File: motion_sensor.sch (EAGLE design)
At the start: 11 parts, among them U1 LP2985A-33DBVTE4

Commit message: Move away from esp8266 to ATMEGA328 + nRF8001
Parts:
- removed MDL1: (no value), ESP8266-ESP12E:ESP8266-12EESP8266-ESP12E
- added C1, C13, C14, C2: 15pF, microbuilder:CAP_CERAMIC0805-NOOUTLINE
- added C10: 0.1uF, microbuilder:CAP_CERAMIC0805-NOOUTLINE
- added C11: 33nF, microbuilder:CAP_CERAMIC0805-NOOUTLINE
- added C12, C4: 0.1µF, microbuilder:CAP_CERAMIC0805-NOOUTLINE
- added C15: 1.5pF, microbuilder:CAP_CERAMIC_0402MP
- added C16, C18: 22pF, SparkFun-Capacitors:22PF-50V-5%(0603)
- added C17, C9: 10µF, microbuilder:CAP_CERAMIC0805-NOOUTLINE
- added C3: 2.2nF, microbuilder:CAP_CERAMIC_0402
- added C5: 1.8pF, microbuilder:CAP_CERAMIC_0402MP
- added C6: 1.2pF, microbuilder:CAP_CERAMIC_0402MP
- added C7: 1µF, microbuilder:CAP_CERAMIC0805-NOOUTLINE
- added C8: 1nF, microbuilder:CAP_CERAMIC_0603
- added FB1: MMZ1608B121C, microbuilder:FERRITE0805
- added J1: AVR_SPI_PRG_6PTH, SparkFun-Connectors:AVR_SPI_PRG_6PTH
- added L1: 8.2nH, microbuilder:INDUCTOR_0402
- added L2: 5.6nH, microbuilder:INDUCTOR_0402
- added L3: 3.9nH, microbuilder:INDUCTOR_0402
- added L4: 10µH, microbuilder:INDUCTOR_0603
- added L5: 15nH, microbuilder:INDUCTOR_0603
- added R1: 22K, microbuilder:RESISTOR_0805MP
- added R2: 10K, SparkFun-Resistors:10KOHM-1/10W-1%(0603)0603
- added U$28: (no value), microbuilder:ANTENNA_PCBNRF8001_1.6MM
- added U2: nRF8001, microbuilder:NRF8001
- added U3: ATMEGA328P_TQFP, SparkFun-DigitalIC:ATMEGA328P_TQFP
- added Y1: 16MHz, microbuilder:CRYSTAL3.2X2.5
- added Y2: FC-255 32.7680K-A3, microbuilder:CRYSTAL8.0X3.8
- added Y3: (no value), SparkFun-FreqCtrl:CRYSTALSMD
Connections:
- removed net ADC: MDL1.ADC
- removed net RX: MDL1.RXD
- removed net TX: MDL1.TXD
- new net 5V: J1.2
- new net ACTIVE: U2A.ACTIVE
- new net AVDD: C4.1, C7.1, C8.1, FB1.P$2, L5.2, U2A.AVDD@1, U2A.AVDD@2, U2A.AVDD@3
- new net MISO: J1.1, U2A.MISO, U3.PB4(MISO)
- new net MOSI: J1.4, U3.PB3(MOSI/OC2)
- new net MOSI_3V: U2A.MOSI
- new net N$1: C11.1, U2A.DEC2
- new net N$10: C2.1, U2A.XC2, Y1.1
- new net N$11: L4.1, U2A.DCC
- new net N$17: L1.2, L3.1, U2A.ANT2
- new net N$18: L1.1, L2.1, U2A.ANT1
- new net N$19: C5.2, L3.2
- new net N$2: R1.1, U2A.IREF
- new net N$20: C15.2, C5.1, C6.2, U$28.P$1
- new net N$21: C16.1, U3.PB6(XTAL1/TOSC1), Y3.1
- new net N$22: C14.2, U2A.XL2, Y2.1
- new net N$23: C13.2, U2A.XL1, Y2.2
- new net N$26: R2.2, U3.PC6(/RESET)
- new net N$3: L4.2, L5.1
- new net N$4: C3.1, L2.2, U2A.VDD_PA
- new net N$8: C10.1, U2A.DEC1
- new net N$9: C1.1, U2A.XC1, Y1.2
- new net RDYN: U2A.RDYN
- new net REQN_3V: U2A.REQN
- new net RESET_3V: U2A.RESET
- new net SCK: J1.3, U3.PB5(SCK)
- new net SCK_3V: U2A.SCK
- net 3.3V: now also C12.1, C17.1, C9.1, FB1.P$1, R2.1, U2A.VDD@1, U2A.VDD@2, U3.AVCC, U3.VCC@4, U3.VCC@6; no longer MDL1.VCC
- net GND: now also C1.2, C10.2, C11.2, C12.2, C13.1, C14.1, C15.1, C16.2, C17.2, C18.2, C2.2, C3.2, C4.2, C6.1, C7.2, C8.2, C9.2, J1.6, R1.2, U2-SLUG.TP, U2A.VSS@1, U2A.VSS@2, U2A.VSS@3, U2A.VSS@4, U2A.VSS@5, U2A.VSS@6, U3.AGND, U3.GND@3, U3.GND@5; no longer MDL1.GND
- net LEDS: no longer MDL1.GPIO13
- net N$16: now also C18.1, U3.PB7(XTAL2/TOSC2), Y3.2; no longer MDL1.GPIO15
- net RESET: now also J1.5; no longer MDL1.REST
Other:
- note added: "Analog Supply Filtering"
- note added: "SPI MODE 0"
- note added: "but RDYN and REQN"
- note added: "replace CS"

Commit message: First PCB attempt
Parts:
- removed C17: 10µF, microbuilder:CAP_CERAMIC0805-NOOUTLINE
- removed D1, D2, D3, D4, D5, D6, D7, D8: (no value), SparkFun-LED:WS2812B
- removed Y3: (no value), SparkFun-FreqCtrl:CRYSTALSMD
- added C19, C20, C24: 0.1uF, SparkFun-Capacitors:0.1UF-25V(+80/-20%)(0603)
- added C21: 2.2uF, SparkFun-Capacitors:2.2UF-10V-20%(0603)
- added C22: 10nF, SparkFun-Capacitors:10NF/10000PF-50V-10%(0603)
- added C23: (no value), SparkFun-Capacitors:1UF-25V-10%(0805)"
- added D9: 250mA/100V, SparkFun-DiscreteSemi:DIODEBAS16
- added U$1, U$11, U$15, U$17: SK6812MINI, pimoroni-optoelectronics:SK6812MINI
- added Y4: 16MHz, microbuilder:CRYSTAL3.2X2.5
- C1, C10, C11, C12, C13, C14, C2, C4, C7, C9: device microbuilder:CAP_CERAMIC0805-NOOUTLINE -> SparkFun-Capacitors:CAP0805
- C15, C5, C6: device microbuilder:CAP_CERAMIC_0402MP -> SparkFun-Capacitors:CAP0805
- C3: device microbuilder:CAP_CERAMIC_0402 -> SparkFun-Capacitors:CAP0805
- C8: device microbuilder:CAP_CERAMIC_0603 -> SparkFun-Capacitors:CAP0805
- R1: device microbuilder:RESISTOR_0805MP -> SparkFun-Resistors:RESISTOR0603-RES
- R2: device SparkFun-Resistors:10KOHM-1/10W-1%(0603)0603 -> SparkFun-Resistors:RESISTOR0603-RES
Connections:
- removed net LEDS: D8.DIN
- removed net MOSI_3V: U2A.MOSI
- removed net N$13: D6.DIN, D7.DOUT
- removed net N$14: D7.DIN, D8.DOUT
- removed net N$15: D4.DIN, D5.DOUT
- removed net N$16: C18.1, U3.PB7(XTAL2/TOSC2), Y3.2
- removed net N$21: C16.1, U3.PB6(XTAL1/TOSC1), Y3.1
- removed net RDYN: U2A.RDYN
- removed net REQN_3V: U2A.REQN
- removed net RESET_3V: U2A.RESET
- removed net SCK_3V: U2A.SCK
- removed net VDD: D1.VDD, D2.VDD, D3.VDD, D4.VDD, D5.VDD, D6.VDD, D7.VDD, D8.VDD, U1.VIN
- new net BLE_RDY: U2A.RDYN, U3.PD2(INT0)
- new net BLE_RST: U2A.RESET, U3.PB1(OC1A)
- new net LED: U$1.DI, U3.PD5(T1)
- new net N$24: C19.1, U3.AREF
- new net N$27: C22.1, U1.BYPASS
- new net OSC1: C16.1, U3.PB6(XTAL1/TOSC1), Y4.1
- new net OSC2: C18.1, U3.PB7(XTAL2/TOSC2), Y4.2
- new net REQN: U2A.REQN, U3.PB2(SS/OC1B)
- new net RX: U3.PD0(RXD)
- new net TX: U3.PD1(TXD)
- new net V_BATT: BAT1.-, C23.1, D9.A, U1.ON/OFF, U1.VIN
- net 3.3V: now also C20.1, C21.1, C24.1; no longer C17.1
- net 5V: now also D9.C, U$1.VDD, U$11.VDD, U$15.VDD, U$17.VDD
- net GND: now also BAT1.+, C19.2, C20.2, C21.2, C22.2, C23.2, C24.2, U$1.GND, U$11.GND, U$15.GND, U$17.GND, U3.PD6(AIN0); no longer C17.2, D1.VSS, D2.VSS, D3.VSS, D4.VSS, D5.VSS, D6.VSS, D7.VSS, D8.VSS
- net MOSI: now also U2A.MOSI
- net N$12: now also U$17.DO; no longer D5.DIN, D6.DOUT
- net N$5: now also U$1.DO, U$11.DI; no longer D1.DIN, D2.DOUT
- net N$6: now also U$11.DO, U$15.DI; no longer D2.DIN, D3.DOUT
- net N$7: now also U$15.DO, U$17.DI; no longer D3.DIN, D4.DOUT
- net SCK: now also U2A.SCK

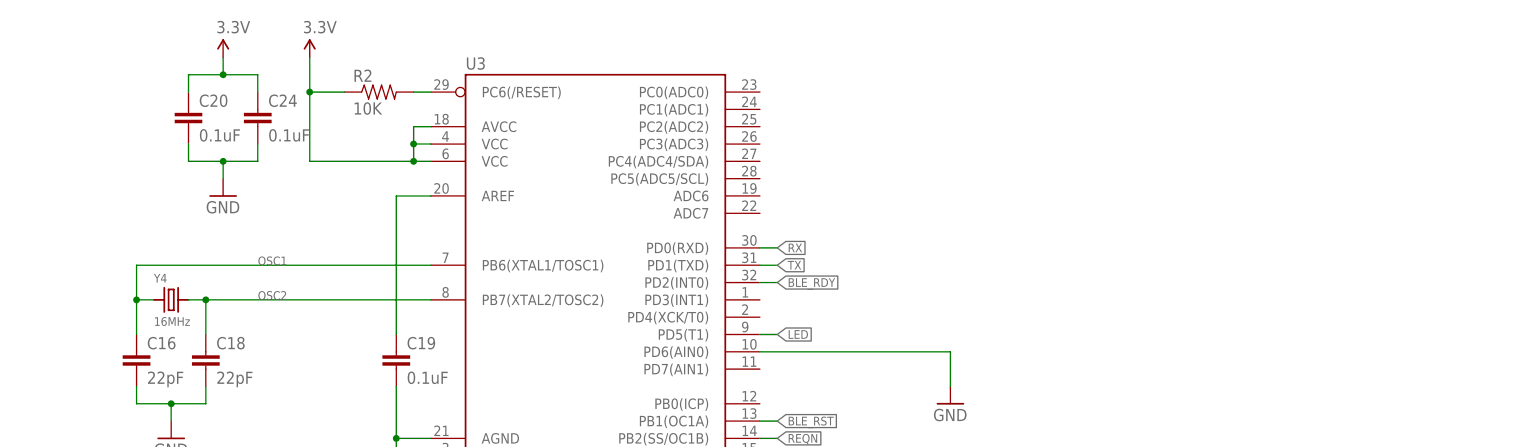
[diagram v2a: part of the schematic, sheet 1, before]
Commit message: Fixing bug with reset circuit. Add FTDI header.
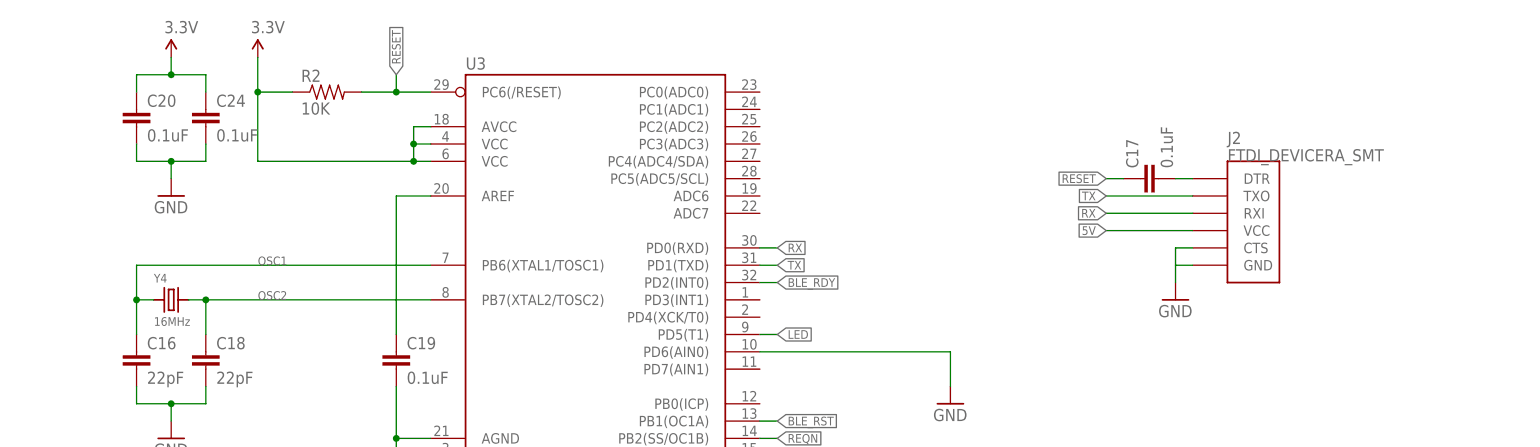
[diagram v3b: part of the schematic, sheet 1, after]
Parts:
- added C17: 0.1uF, SparkFun-Capacitors:0.1UF-25V(+80/-20%)(0603)
- added J2: FTDI_DEVICERA_SMT, SparkFun-Connectors:FTDI_DEVICERA_SMT
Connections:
- removed net N$26: R2.2, U3.PC6(/RESET)
- new net DTR: C17.2, J2.DTR
- net 5V: now also J2.VCC
- net GND: now also J2.CTS, J2.GND
- net RESET: now also C17.1, R2.2, U3.PC6(/RESET)
- net RX: now also J2.RXI
- net TX: now also J2.TXO
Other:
- moved on the sheet: C20, C24, R2
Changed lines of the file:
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@@
 <part name="C24" library="SparkFun-Capacitors" deviceset="0.1UF-25V(+80/-20%)(0603)" device="" value="0.1uF"/>
 <part name="GND16" library="SparkFun-Aesthetics" deviceset="GND" device=""/>
+<part name="J2" library="SparkFun-Connectors" deviceset="FTDI_DEVICE" device="RA_SMT" value="FTDI_DEVICERA_SMT"/>
+<part name="GND17" library="SparkFun-Aesthetics" deviceset="GND" device=""/>
+<part name="C17" library="SparkFun-Capacitors" deviceset="0.1UF-25V(+80/-20%)(0603)" device="" value="0.1uF"/>
 </parts>
 <sheets>
@@
 <instance part="GND10" gate="1" x="33.02" y="104.14"/>
 <instance part="GND12" gate="1" x="66.04" y="91.44"/>
-<instance part="SUPPLY9" gate="G$1" x="53.34" y="160.02"/>
-<instance part="R2" gate="G$1" x="63.5" y="154.94"/>
+<instance part="SUPPLY9" gate="G$1" x="45.72" y="160.02"/>
+<instance part="R2" gate="G$1" x="55.88" y="154.94"/>
 <instance part="J1" gate="G$1" x="93.98" y="71.12"/>
 <instance part="SUPPLY16" gate="G$1" x="111.76" y="76.2"/>
 <instance part="GND13" gate="1" x="111.76" y="60.96"/>
 <instance part="C19" gate="G$1" x="66.04" y="114.3"/>
-<instance part="C20" gate="G$1" x="35.56" y="149.86"/>
-<instance part="SUPPLY17" gate="G$1" x="40.64" y="160.02"/>
-<instance part="GND14" gate="1" x="40.64" y="139.7"/>
+<instance part="C20" gate="G$1" x="27.94" y="149.86"/>
+<instance part="SUPPLY17" gate="G$1" x="33.02" y="160.02"/>
+<instance part="GND14" gate="1" x="33.02" y="139.7"/>
 <instance part="SUPPLY18" gate="G$1" x="38.1" y="73.66"/>
 <instance part="U$1" gate="G$1" x="45.72" y="38.1"/>
@@
 <instance part="C23" gate="G$1" x="266.7" y="96.52"/>
 <instance part="SUPPLY10" gate="G$1" x="281.94" y="109.22"/>
-<instance part="C24" gate="G$1" x="45.72" y="149.86"/>
+<instance part="C24" gate="G$1" x="38.1" y="149.86"/>
 <instance part="GND16" gate="1" x="147.32" y="109.22"/>
+<instance part="J2" gate="G$1" x="187.96" y="137.16"/>
+<instance part="GND17" gate="1" x="180.34" y="124.46"/>
+<instance part="C17" gate="G$1" x="177.8" y="142.24" rot="R90"/>
 </instances>
 <busses>
@@
 <pinref part="C20" gate="G$1" pin="2"/>
 <pinref part="GND14" gate="1" pin="GND"/>
-<wire x1="35.56" y1="147.32" x2="35.56" y2="144.78" width="0.1524" layer="91"/>
-<wire x1="35.56" y1="144.78" x2="40.64" y2="144.78" width="0.1524" layer="91"/>
-<wire x1="40.64" y1="144.78" x2="40.64" y2="142.24" width="0.1524" layer="91"/>
-<wire x1="40.64" y1="144.78" x2="45.72" y2="144.78" width="0.1524" layer="91"/>
+<wire x1="27.94" y1="147.32" x2="27.94" y2="144.78" width="0.1524" layer="91"/>
+<wire x1="27.94" y1="144.78" x2="33.02" y2="144.78" width="0.1524" layer="91"/>
+<wire x1="33.02" y1="144.78" x2="33.02" y2="142.24" width="0.1524" layer="91"/>
+<wire x1="33.02" y1="144.78" x2="38.1" y2="144.78" width="0.1524" layer="91"/>
 <pinref part="C24" gate="G$1" pin="2"/>
-<wire x1="45.72" y1="144.78" x2="45.72" y2="147.32" width="0.1524" layer="91"/>
-<junction x="40.64" y="144.78"/>
+<wire x1="38.1" y1="144.78" x2="38.1" y2="147.32" width="0.1524" layer="91"/>
+<junction x="33.02" y="144.78"/>
 </segment>
 <segment>
@@
 <wire x1="119.38" y1="116.84" x2="147.32" y2="116.84" width="0.1524" layer="91"/>
 <wire x1="147.32" y1="116.84" x2="147.32" y2="111.76" width="0.1524" layer="91"/>
+</segment>
+<segment>
+<pinref part="J2" gate="G$1" pin="GND"/>
+<wire x1="182.88" y1="129.54" x2="180.34" y2="129.54" width="0.1524" layer="91"/>
+<wire x1="180.34" y1="129.54" x2="180.34" y2="127" width="0.1524" layer="91"/>
+<pinref part="GND17" gate="1" pin="GND"/>
+<pinref part="J2" gate="G$1" pin="CTS"/>
+<wire x1="182.88" y1="132.08" x2="180.34" y2="132.08" width="0.1524" layer="91"/>
+<wire x1="180.34" y1="132.08" x2="180.34" y2="129.54" width="0.1524" layer="91"/>
 </segment>
 </net>
@@
 <pinref part="SUPPLY9" gate="G$1" pin="3.3V"/>
 <wire x1="71.12" y1="144.78" x2="68.58" y2="144.78" width="0.1524" layer="91"/>
-<wire x1="68.58" y1="144.78" x2="53.34" y2="144.78" width="0.1524" layer="91"/>
-<wire x1="53.34" y1="144.78" x2="53.34" y2="154.94" width="0.1524" layer="91"/>
+<wire x1="68.58" y1="144.78" x2="45.72" y2="144.78" width="0.1524" layer="91"/>
+<wire x1="45.72" y1="144.78" x2="45.72" y2="154.94" width="0.1524" layer="91"/>
 <pinref part="U3" gate="U$1" pin="VCC@4"/>
-<wire x1="53.34" y1="154.94" x2="53.34" y2="160.02" width="0.1524" layer="91"/>
+<wire x1="45.72" y1="154.94" x2="45.72" y2="160.02" width="0.1524" layer="91"/>
 <wire x1="71.12" y1="147.32" x2="68.58" y2="147.32" width="0.1524" layer="91"/>
 <wire x1="68.58" y1="147.32" x2="68.58" y2="144.78" width="0.1524" layer="91"/>
@@
 <junction x="68.58" y="147.32"/>
 <pinref part="R2" gate="G$1" pin="1"/>
-<wire x1="58.42" y1="154.94" x2="53.34" y2="154.94" width="0.1524" layer="91"/>
-<junction x="53.34" y="154.94"/>
+<wire x1="50.8" y1="154.94" x2="45.72" y2="154.94" width="0.1524" layer="91"/>
+<junction x="45.72" y="154.94"/>
 </segment>
 <segment>
 <pinref part="SUPPLY17" gate="G$1" pin="3.3V"/>
 <pinref part="C20" gate="G$1" pin="1"/>
-<wire x1="35.56" y1="154.94" x2="35.56" y2="157.48" width="0.1524" layer="91"/>
-<wire x1="35.56" y1="157.48" x2="40.64" y2="157.48" width="0.1524" layer="91"/>
-<wire x1="40.64" y1="157.48" x2="40.64" y2="160.02" width="0.1524" layer="91"/>
-<wire x1="40.64" y1="157.48" x2="45.72" y2="157.48" width="0.1524" layer="91"/>
+<wire x1="27.94" y1="154.94" x2="27.94" y2="157.48" width="0.1524" layer="91"/>
+<wire x1="27.94" y1="157.48" x2="33.02" y2="157.48" width="0.1524" layer="91"/>
+<wire x1="33.02" y1="157.48" x2="33.02" y2="160.02" width="0.1524" layer="91"/>
+<wire x1="33.02" y1="157.48" x2="38.1" y2="157.48" width="0.1524" layer="91"/>
 <pinref part="C24" gate="G$1" pin="1"/>
-<wire x1="45.72" y1="157.48" x2="45.72" y2="154.94" width="0.1524" layer="91"/>
-<junction x="40.64" y="157.48"/>
+<wire x1="38.1" y1="157.48" x2="38.1" y2="154.94" width="0.1524" layer="91"/>
+<junction x="33.02" y="157.48"/>
 </segment>
 </net>
@@
 </segment>
 </net>
-<net name="N$26" class="0">
-<segment>
-<pinref part="R2" gate="G$1" pin="2"/>
-<pinref part="U3" gate="U$1" pin="PC6(/RESET)"/>
-<wire x1="68.58" y1="154.94" x2="71.12" y2="154.94" width="0.1524" layer="91"/>
-</segment>
-</net>
 <net name="SCK" class="0">
 <segment>
@@
 <wire x1="86.36" y1="68.58" x2="78.74" y2="68.58" width="0.1524" layer="91"/>
 <label x="78.74" y="68.58" size="1.27" layer="95" rot="R180" xref="yes"/>
+</segment>
+<segment>
+<pinref part="C17" gate="G$1" pin="1"/>
+<wire x1="172.72" y1="142.24" x2="170.18" y2="142.24" width="0.1524" layer="91"/>
+<label x="170.18" y="142.24" size="1.27" layer="95" rot="R180" xref="yes"/>
+</segment>
+<segment>
+<pinref part="R2" gate="G$1" pin="2"/>
+<pinref part="U3" gate="U$1" pin="PC6(/RESET)"/>
+<wire x1="60.96" y1="154.94" x2="66.04" y2="154.94" width="0.1524" layer="91"/>
+<wire x1="66.04" y1="154.94" x2="71.12" y2="154.94" width="0.1524" layer="91"/>
+<wire x1="66.04" y1="154.94" x2="66.04" y2="157.48" width="0.1524" layer="91"/>
+<junction x="66.04" y="154.94"/>
+<label x="66.04" y="157.48" size="1.27" layer="95" rot="R90" xref="yes"/>
 </segment>
 </net>
@@
 <pinref part="SUPPLY8" gate="G$1" pin="5V"/>
 <wire x1="152.4" y1="48.26" x2="152.4" y2="45.72" width="0.1524" layer="91"/>
+</segment>
+<segment>
+<pinref part="J2" gate="G$1" pin="VCC"/>
+<wire x1="182.88" y1="134.62" x2="170.18" y2="134.62" width="0.1524" layer="91"/>
+<label x="170.18" y="134.62" size="1.27" layer="95" rot="R180" xref="yes"/>
 </segment>
 </net>
@@
 <label x="121.92" y="129.54" size="1.27" layer="95" xref="yes"/>
 </segment>
+<segment>
+<pinref part="J2" gate="G$1" pin="TXO"/>
+<wire x1="182.88" y1="139.7" x2="170.18" y2="139.7" width="0.1524" layer="91"/>
+<label x="170.18" y="139.7" size="1.27" layer="95" rot="R180" xref="yes"/>
+</segment>
 </net>
 <net name="RX" class="0">
@@
 <label x="121.92" y="132.08" size="1.27" layer="95" xref="yes"/>
 </segment>
-</net>
+<segment>
+<pinref part="J2" gate="G$1" pin="RXI"/>
+<wire x1="170.18" y1="137.16" x2="182.88" y2="137.16" width="0.1524" layer="91"/>
+<label x="170.18" y="137.16" size="1.27" layer="95" rot="R180" xref="yes"/>
+</segment>
+</net>
+<net name="DTR" class="0">
+<segment>
+<pinref part="J2" gate="G$1" pin="DTR"/>
+<pinref part="C17" gate="G$1" pin="2"/>
+<wire x1="180.34" y1="142.24" x2="182.88" y2="142.24" width="0.1524" layer="91"/>
+</segment>
+</net>
